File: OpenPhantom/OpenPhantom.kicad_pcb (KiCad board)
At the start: 2 copper layers, 175 x 175 mm, 107 parts, among them J1 Barrel_Jack, J2 Video, J3 Audio, Q1 BC548, Q2 BD136, Q3 BC557, Q4 BC548, SW1 POWER, SW2 RESET, U1 UM6116 VRAM, U10 74HC368, U11 74HC368, U2 UM6116 WRAM, U3 74HC04, U4 UA6547_CPU, U5 4013, U6 UA6548_PPU, U7 74HC139, U8 74LS373, U9 LM7805_TO220, Y1 21.453366 MHz

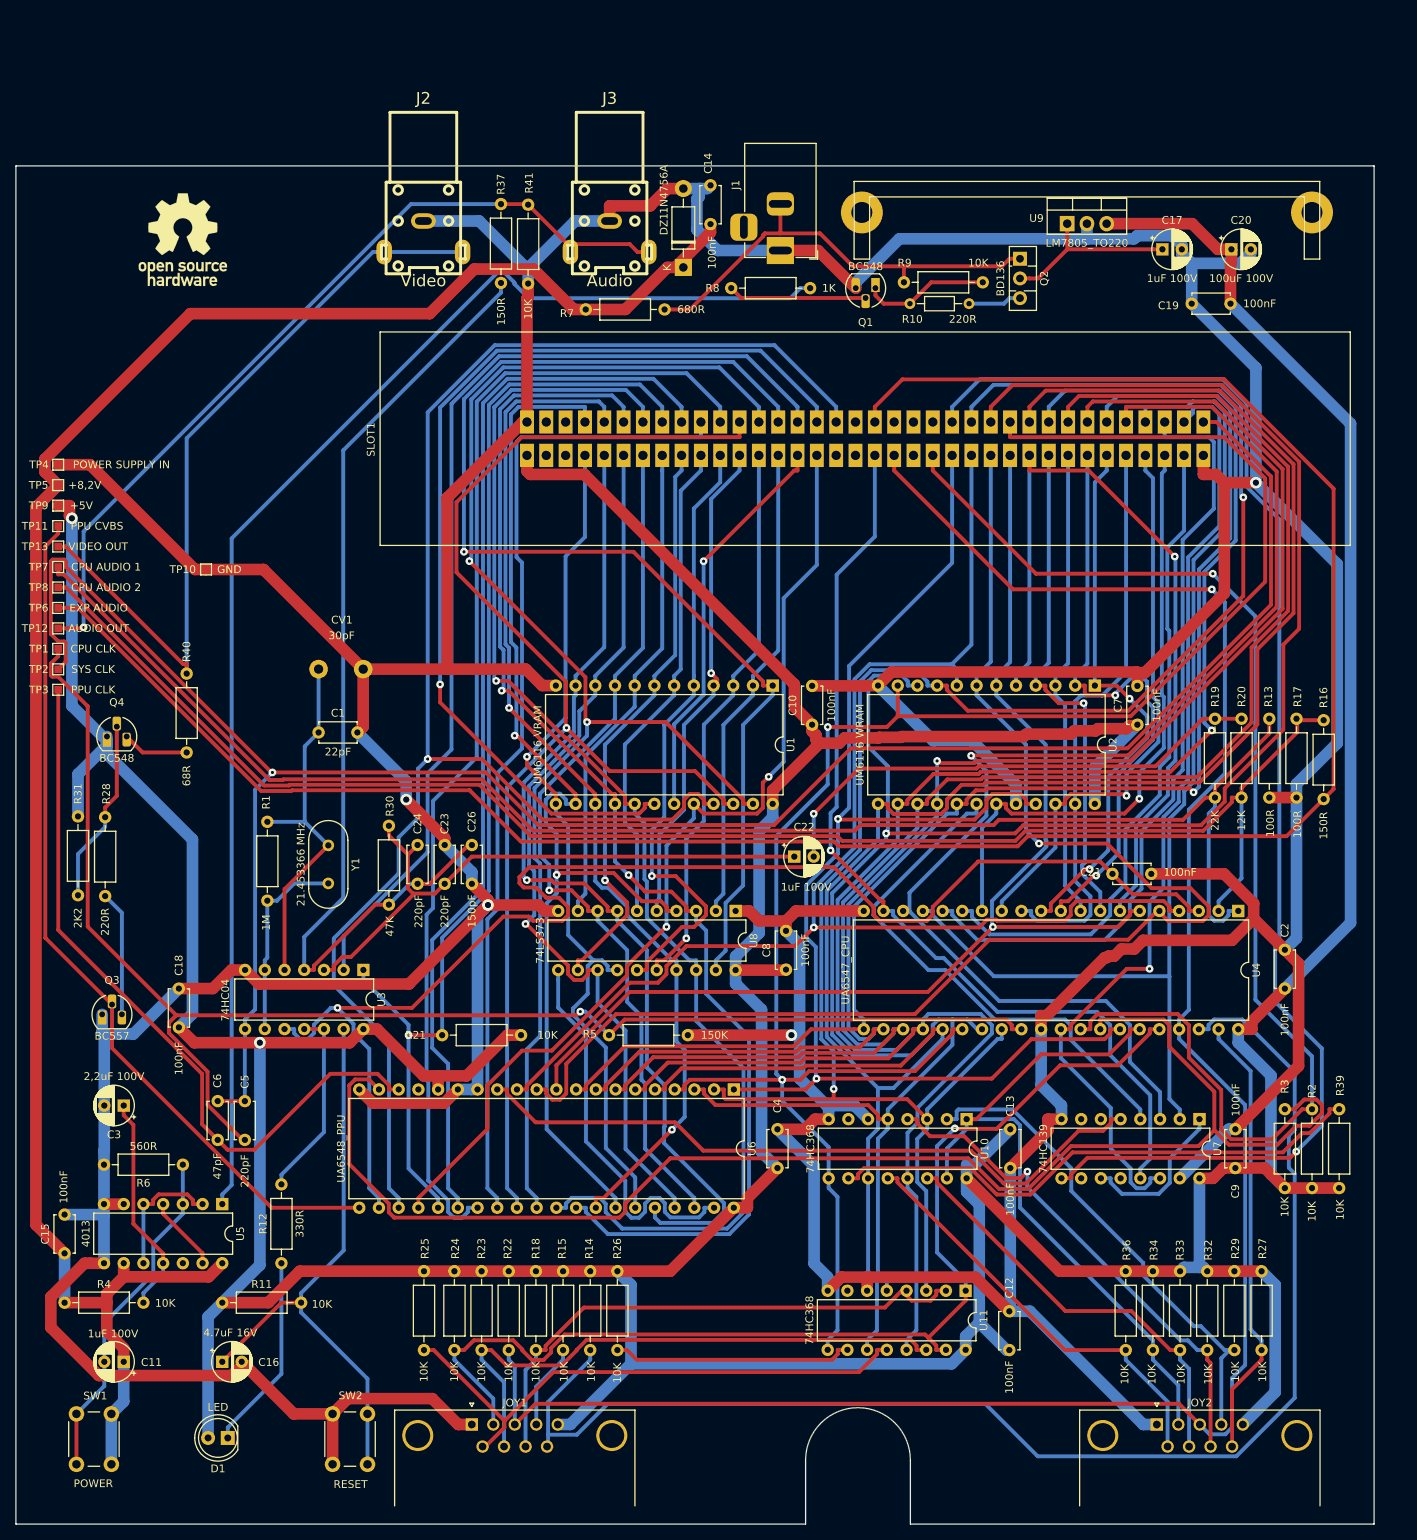
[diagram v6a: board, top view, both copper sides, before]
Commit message: Added R35
Added R35 to improved image quality.
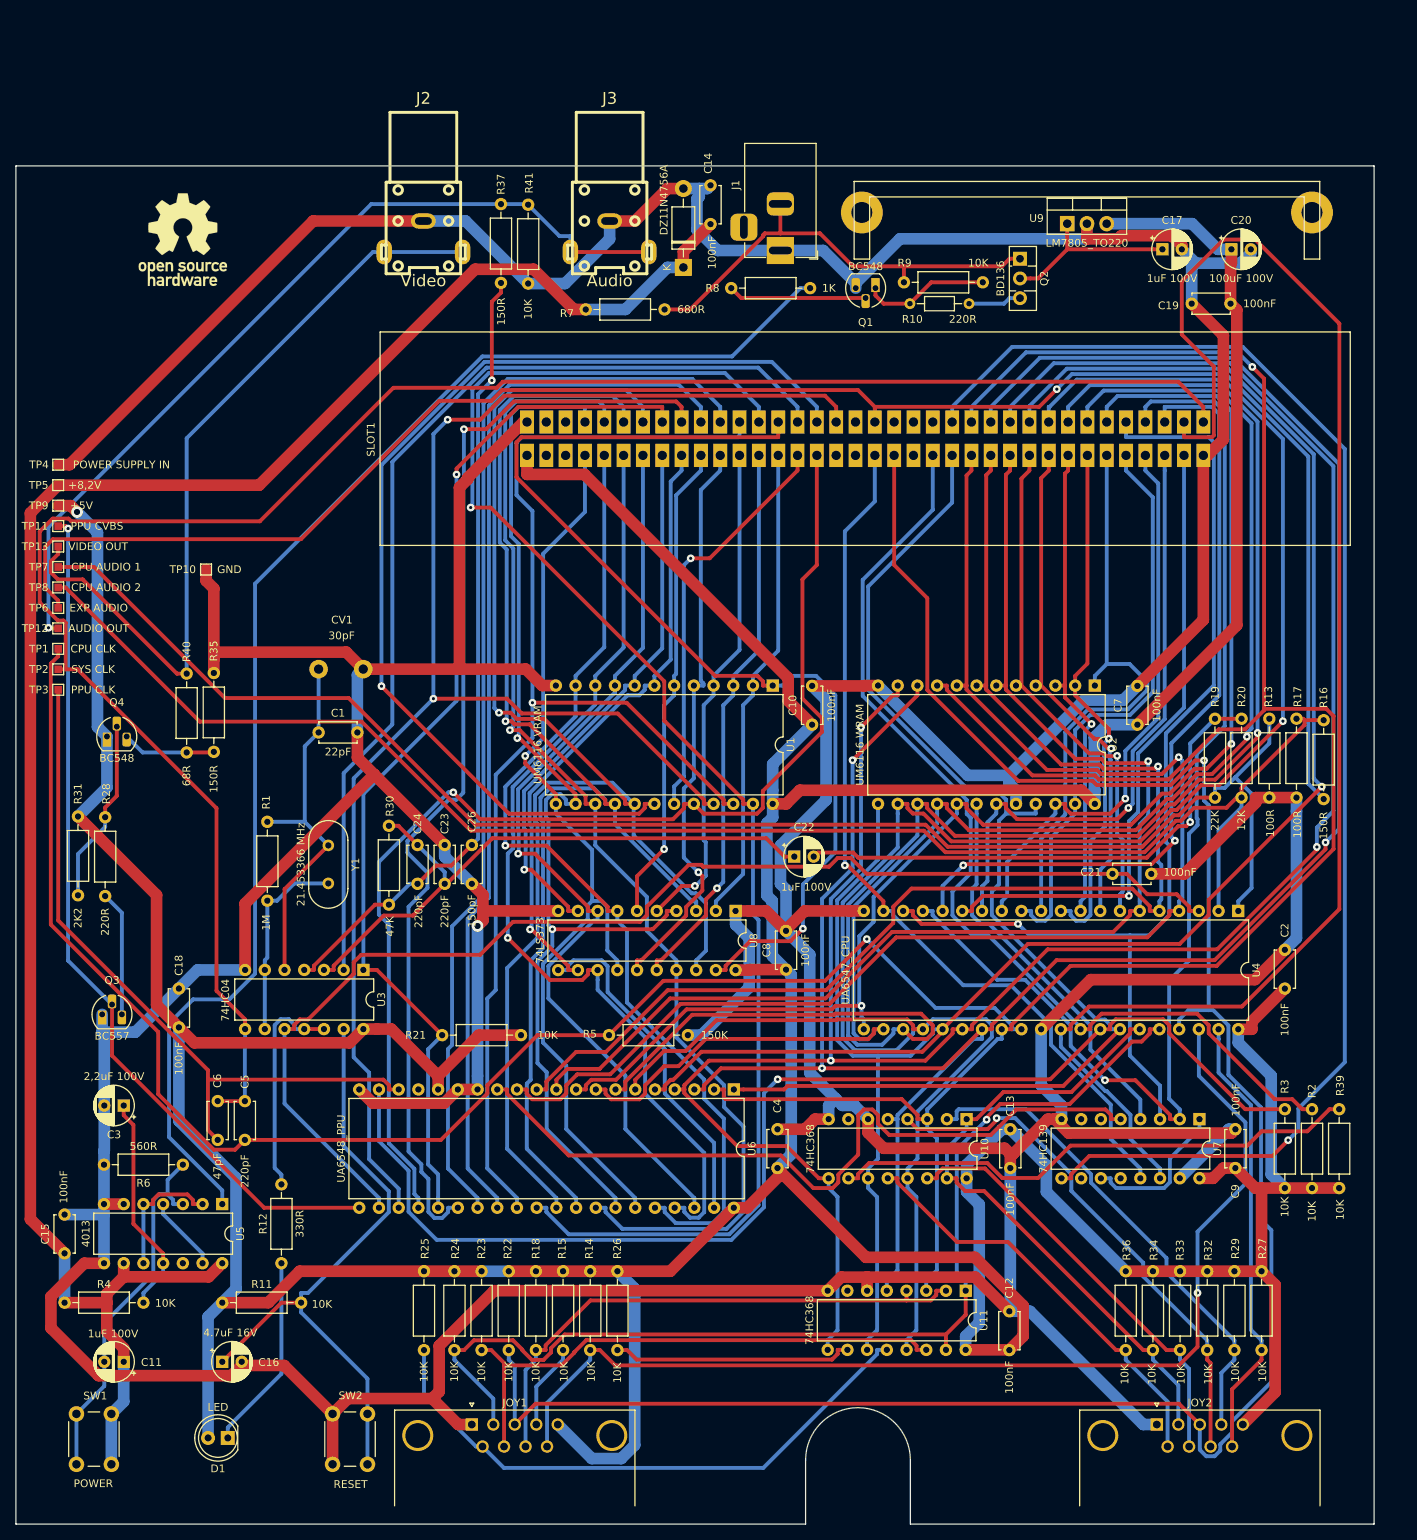
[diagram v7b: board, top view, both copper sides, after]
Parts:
- added R35: 150R, Resistor_THT:R_Axial_DIN0207_L6.3mm_D2.5mm_P10.16mm_Horizontal, F.Cu at (42.0, 101.5)
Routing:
- net /M2: track 124.6 -> 197.1 mm, vias 1 -> 0
- net /EXP-6: track 287.3 -> 233.6 mm, vias 0 -> 1
- net /CPU-D2: track 246.1 -> 297.2 mm, vias 2 -> 3
- net /GND: track 1028.7 -> 1074.8 mm, vias 4 -> 1
- net /CPU-D0: track 247.7 -> 286.0 mm, vias 2 -> 1
- net /CPU-A3: track 104.3 -> 67.3 mm
- net /OUT-1: track 177.1 -> 140.7 mm, vias 0 -> 1
- net /~{IRQ}: track 162.8 -> 129.1 mm, vias 1 -> 0
- net /VCC: track 809.9 -> 776.6 mm, vias 2 -> 1
- net /~{NMI}: track 187.7 -> 157.9 mm, vias 0 -> 1
- net /PPU-~{RD}: track 127.0 -> 153.6 mm, vias 2 -> 1
- net Net-(C24-Pad1): track 127.6 -> 102.6 mm, vias 0 -> 1
- net /CPU-A14: track 163.6 -> 139.5 mm
- net /SYSTEM-CLK: track 274.7 -> 251.7 mm, vias 1 -> 0
- net /PPU-D5: track 133.7 -> 154.6 mm, vias 2 -> 1
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
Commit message: Player controller fixed
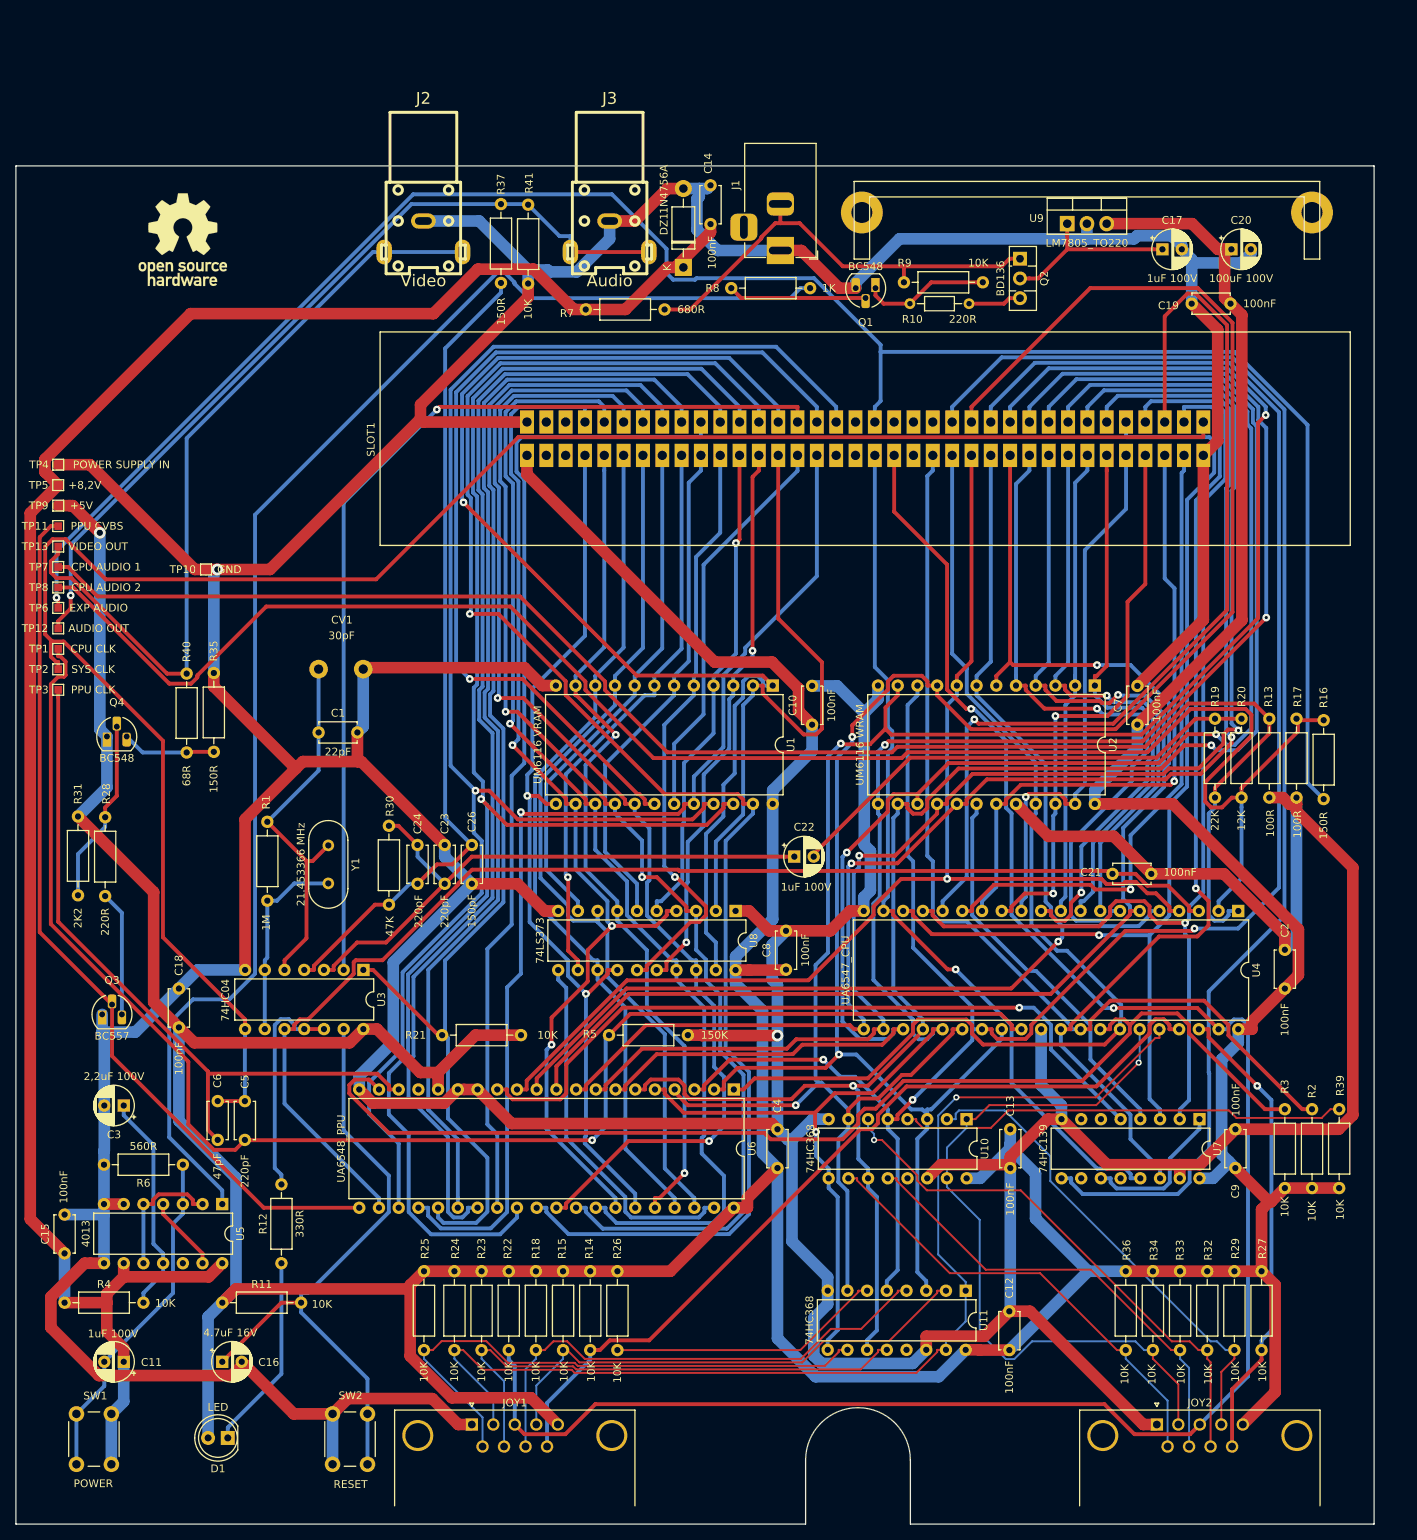
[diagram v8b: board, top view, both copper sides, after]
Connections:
- net /4017-D0 renamed /JOY2-D0
- net /~{OE1} renamed /~{INP0}
- net /~{OE2} renamed /~{INP1}
- JOY1 pad 4: /4016-D0 -> /JOY1-D0
- JOY1 pad 6: /4016-D3 -> /JOY1-D3
- JOY1 pad 7: /4016-D4 -> /JOY1-D4
- JOY1 pad 8: /4016-D1 -> /JOY1-D1
- JOY1 pad 9: /OUT-1 -> /OUT-2
- JOY2 pad 6: /4017-D3 -> /JOY2-D3
- JOY2 pad 7: /4017-D4 -> /JOY2-D4
- JOY2 pad 8: /4017-D1 -> /JOY2-D2
- JOY2 pad 9: /OUT-2 -> /OUT-1
- R14 pad 2: /OUT-1 -> /OUT-2
- R15 pad 2: /4016-D0 -> /JOY1-D0
- R18 pad 2: /4016-D1 -> /JOY1-D1
- R23 pad 2: /4016-D4 -> /JOY1-D4
- R25 pad 2: /4016-D3 -> /JOY1-D3
- R26 pad 2: /4016-D2 -> /JOY1-D2
- R27 pad 2: /OUT-2 -> /OUT-1
- R32 pad 2: /4017-D1 -> /JOY2-D2
- R33 pad 2: /4017-D4 -> /JOY2-D4
- R36 pad 2: /4017-D3 -> /JOY2-D3
- R39 pad 2: /4017-D2 -> /JOY2-D1
- U10 pad 10: /4017-D2 -> /JOY2-D3
- U10 pad 11: /CPU-D3 -> /CPU-D4
- U10 pad 12: /4017-D3 -> /JOY2-D4
- U10 pad 13: /CPU-D4 -> unconnected-(U10-Pad13)
- U10 pad 14: /4017-D4 -> /GND
- U10 pad 4: /4017-D1 -> /JOY2-D1
- U10 pad 6: /GND -> /JOY2-D2
- U10 pad 7: unconnected-(U10-Pad7) -> /CPU-D2
- U10 pad 9: /CPU-D2 -> /CPU-D3
- U11 pad 10: /4016-D2 -> /JOY1-D3
- U11 pad 11: /CPU-D3 -> /CPU-D4
- U11 pad 12: /4016-D3 -> /JOY1-D4
- U11 pad 13: /CPU-D4 -> unconnected-(U11-Pad13)
- U11 pad 14: /4016-D4 -> /GND
- U11 pad 2: /4016-D1 -> /JOY1-D0
- U11 pad 4: /4016-D1 -> /JOY1-D1
- U11 pad 6: /GND -> /JOY1-D2
- U11 pad 7: unconnected-(U11-Pad7) -> /CPU-D2
- U11 pad 9: /CPU-D2 -> /CPU-D3
- U4 pad 37: /EXP-1 -> /OUT-2
- U4 pad 39: /OUT-2 -> /EXP-1
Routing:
- net /OUT-1: track 140.7 -> 60.5 mm
- net /4016-D3: track 75.9 -> 0.00 mm
- net /M2: track 197.1 -> 124.1 mm, vias 0 -> 1
- net /JOY1-D3: track 0.00 -> 72.9 mm
- net /4016-D4: track 71.0 -> 0.00 mm
- net /4016-D1: track 70.9 -> 0.00 mm
- net /JOY2-D2: track 0.00 -> 70.2 mm, vias 0 -> 1
- net /4017-D2: track 68.8 -> 0.00 mm
- net /JOY1-D4: track 0.00 -> 68.1 mm
- net /4017-D1: track 67.9 -> 0.00 mm, vias 1 -> 0
- net /JOY1-D1: track 0.00 -> 65.9 mm
- net /JOY1-D0: track 0.00 -> 65.0 mm
- net /JOY2-D4: track 0.00 -> 59.9 mm
- net /JOY2-D3: track 0.00 -> 59.7 mm
- net /JOY2-D1: track 0.00 -> 58.1 mm
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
